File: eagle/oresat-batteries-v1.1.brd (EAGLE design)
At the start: 98.6 x 95.3 mm, 96 parts, among them IC1 74AHC1G08DBV, J2 CORTEX_DEBUG_PTH, Q1 CSD16340Q3, Q2 CSD16340Q3, Q3 TPN4R712MD, Q4 TPN4R712MD, Q5 TPN4R712MD, Q6 TPN4R712MD, Q7 CSD16340Q3, U1 LM3761, U10 LTC4412, U11 MAX17055, U12 LTC4412, U13 LTC4412, U14 STM32F042K6, U15 TCAN330, U2 MC74HC1G04DFT1GOSCT, U3 BQ2970, U4 LTC4411, U5 LTC4411, U6 LTC4411, U7 LTC4411, U8 MC74HC1G04DFT1GOSCT, U9 LTC4412, X1 16MHz

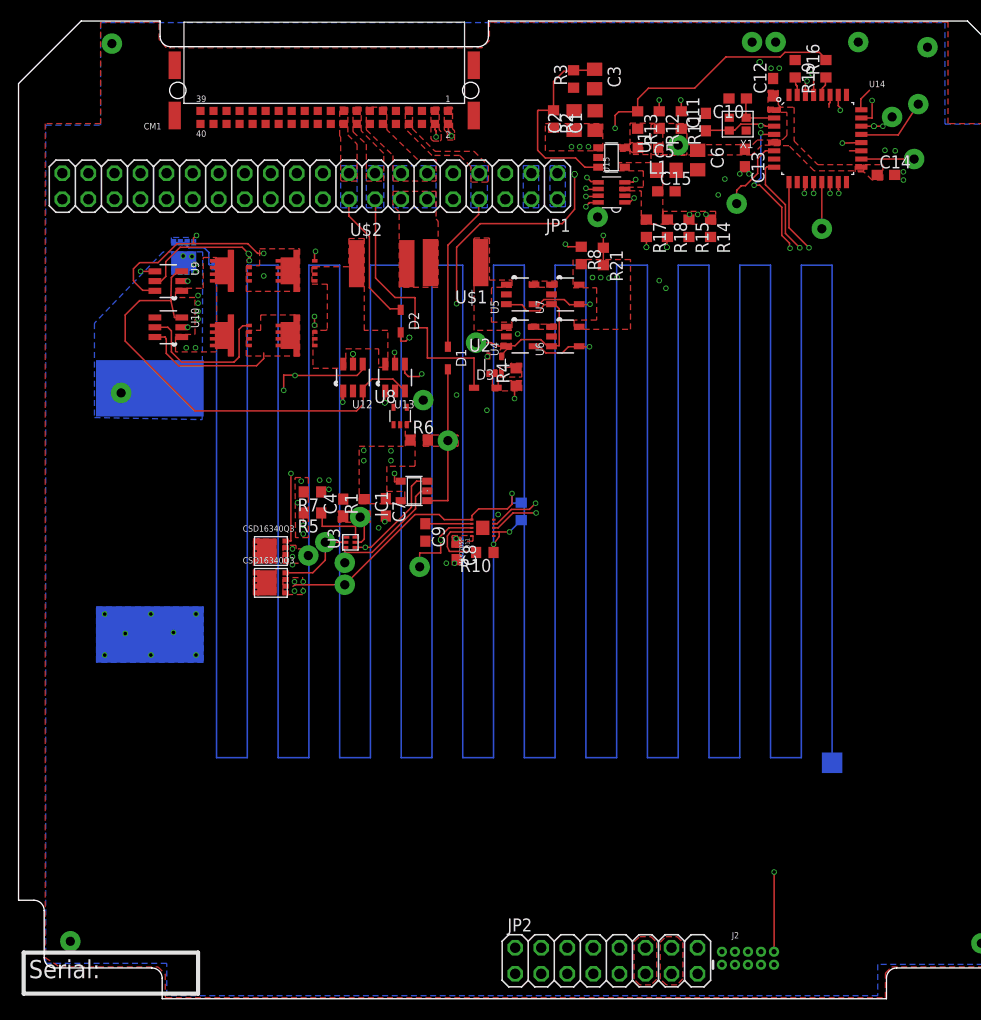
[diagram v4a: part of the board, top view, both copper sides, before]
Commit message: Cosmetics, moved signals to top and bottom layer.
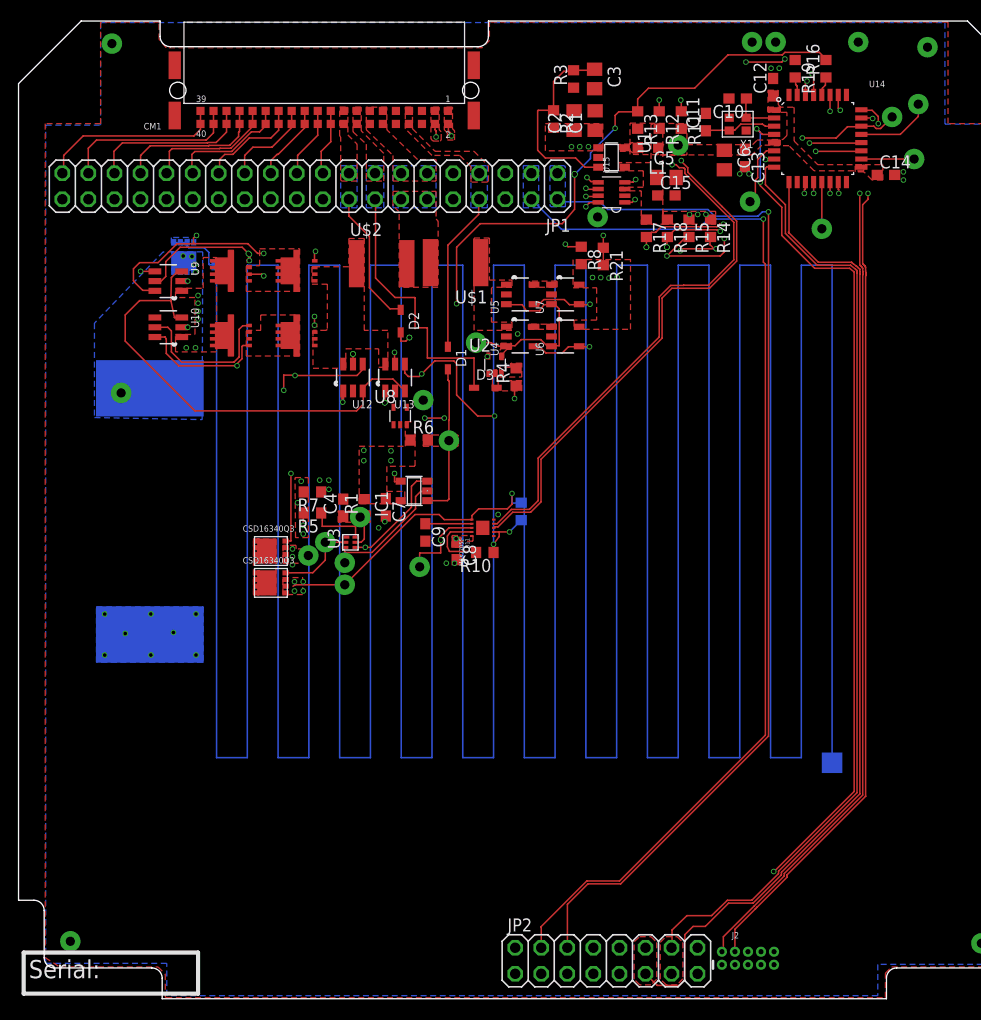
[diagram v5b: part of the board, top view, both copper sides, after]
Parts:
- moved C6 2.60 mm to (68.8, 81.8)
- moved TP24 1.32 mm to (71.3, 77.7)
- moved C5 0.70 mm to (63.1, 80.0)
- moved C15 0.40 mm to (63.1, 78.3)
- moved TP7 0.10 mm to (42.0, 54.4)
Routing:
- net CANH: track 20.3 -> 126.6 mm, vias 2 -> 3
- net CANL: track 17.9 -> 121.1 mm, vias 2 -> 3
- net SPARE11: track 0.00 -> 18.0 mm
- net SPARE10: track 0.00 -> 17.4 mm
- net SPARE9: track 0.00 -> 16.0 mm
- net SPARE8: track 0.00 -> 14.6 mm
- net SPARE7: track 0.00 -> 12.9 mm
- net SPARE6: track 0.00 -> 11.7 mm
- net SPARE5: track 0.00 -> 10.2 mm
- net SDA: track 71.3 -> 80.5 mm, vias 4 -> 3
- net SPARE4: track 0.00 -> 9.06 mm
- net SCL: track 72.7 -> 81.5 mm, vias 6 -> 5
- net SPARE3: track 0.00 -> 7.50 mm
- net SPARE2: track 0.00 -> 6.91 mm
- net SPARE1: track 0.00 -> 6.53 mm
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- added copper zone on layer 15, net 3.3V
- removed copper zone on layer 2, net 3.3V

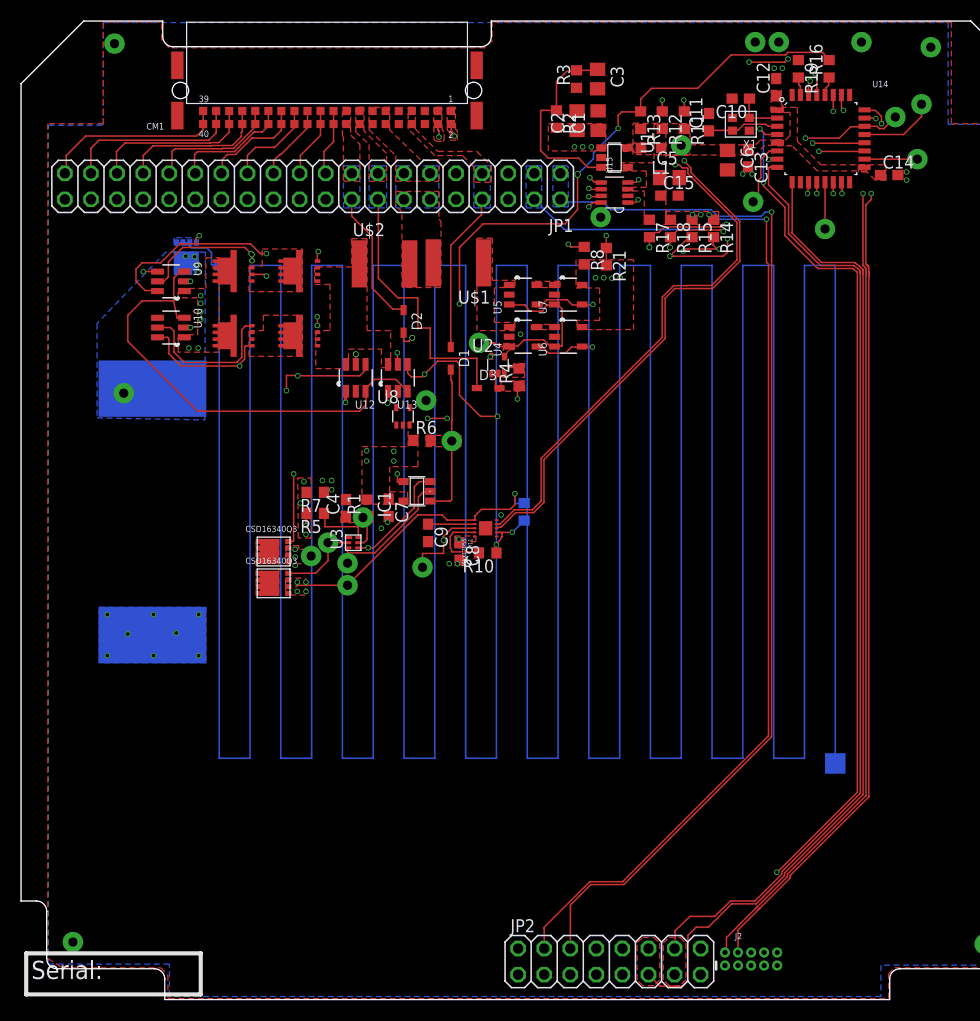
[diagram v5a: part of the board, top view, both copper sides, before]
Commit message: Cosmetics, moved all power and signals from gnd layer
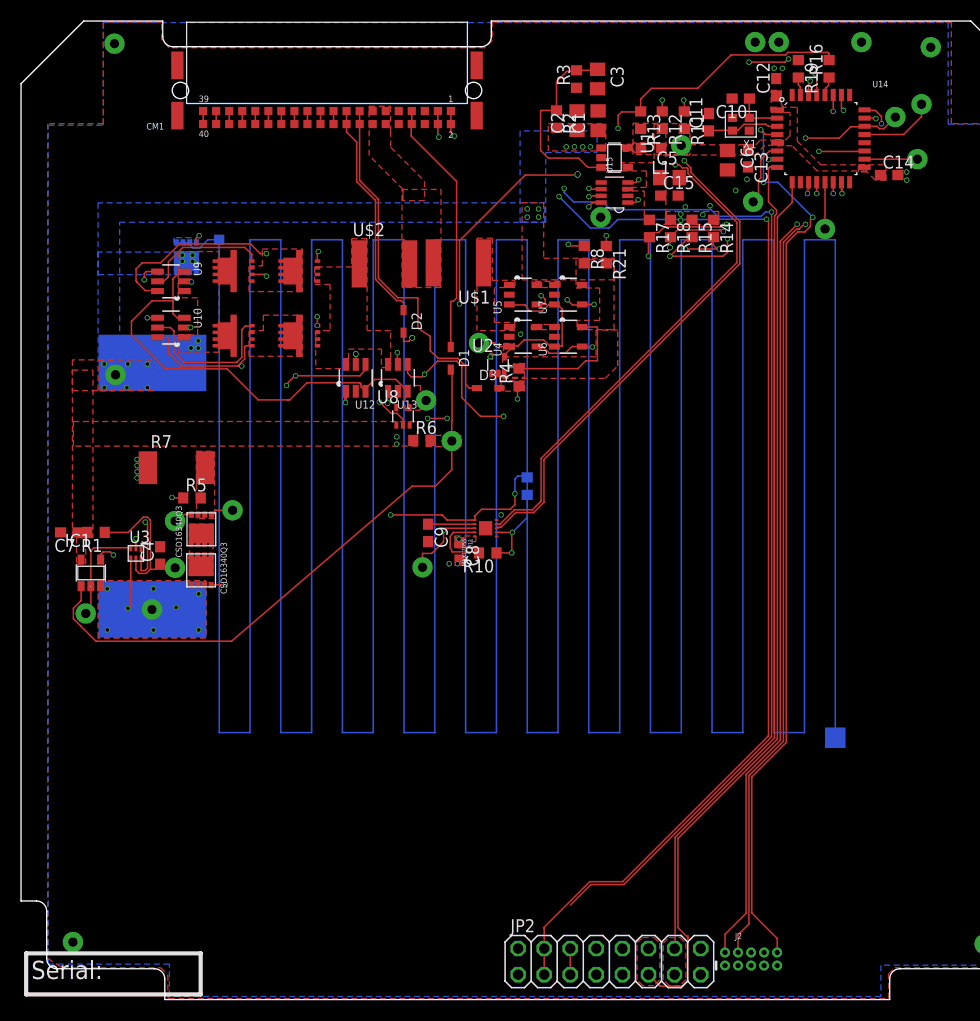
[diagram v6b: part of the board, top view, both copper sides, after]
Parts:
- removed JP1: (no value), pinhead:2X20
- R7: device rcl:R0603 -> rcl:R2512
- moved IC1 32.7 mm to (6.80, 41.5), turned to 0 degrees
- moved C7 31.2 mm to (4.70, 45.5), turned to 180 degrees
- moved R1 26.5 mm to (7.30, 45.5), turned to 180 degrees
- moved TP8 26.0 mm to (6.30, 37.6)
- moved U3 21.2 mm to (11.2, 43.5), turned to 180 degrees
- moved TP5 18.9 mm to (15.0, 42.0)
- moved C4 18.7 mm to (13.6, 43.2)
- moved TP20 16.3 mm to (12.8, 38.0)
- moved TP9 15.0 mm to (15.0, 46.6)
- moved R7 13.7 mm to (15.2, 51.8), turned to 0 degrees
- moved TP13 13.4 mm to (20.6, 47.6)
- moved R5 12.1 mm to (16.6, 48.9), turned to 0 degrees
- moved Q2 8.79 mm to (17.6, 45.8), turned to 180 degrees
- moved Q1 7.30 mm to (17.5, 41.8), turned to 0 degrees
- moved R9 2.52 mm to (49.3, 50.0)
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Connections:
- net !SHUTDOWN: no longer JP1.7, JP1.8
- net CANH: no longer JP1.3, JP1.4
- net CANL: no longer JP1.1, JP1.2
- net CHG_CTL: no longer JP1.15, JP1.16
- net DCHG_CTL: no longer JP1.17, JP1.18
- net GND: no longer JP1.10, JP1.5, JP1.6, JP1.9
- net SPARE1: no longer JP1.19
- net SPARE10: no longer JP1.37
- net SPARE11: no longer JP1.39
- net SPARE2: no longer JP1.21
- net SPARE3: no longer JP1.23
- net SPARE4: no longer JP1.25
- net SPARE5: no longer JP1.27
- net SPARE6: no longer JP1.29
- net SPARE7: no longer JP1.31
- net SPARE8: no longer JP1.33
- net SPARE9: no longer JP1.35
- net VSOLAR: no longer JP1.11, JP1.12, JP1.13, JP1.14
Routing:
- net TO_CHG: track 51.5 -> 117.8 mm
- net SYSSHD: track 14.9 -> 57.3 mm
- net CAN_EN: track 32.0 -> 0.00 mm, vias 2 -> 0
- net SPARE11: track 18.0 -> 1.27 mm
- net SPARE10: track 17.4 -> 1.27 mm
- net SPARE9: track 16.0 -> 1.27 mm
- net SPARE8: track 14.6 -> 1.27 mm
- net V_BATT: track 0.00 -> 13.0 mm, vias 22 -> 24
- net BQBAT: track 3.27 -> 15.6 mm
- net BATT-: track 16.9 -> 4.95 mm, vias 12 -> 8
- net SPARE7: track 12.9 -> 1.27 mm
- net USART2_TX: track 92.8 -> 81.3 mm
- net TO_DCHG: track 58.6 -> 69.8 mm, vias 4 -> 5
- net SPARE6: track 11.7 -> 1.27 mm
- net !SHUTDOWN: track 15.6 -> 25.2 mm
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- added copper zone on layer 1, net DSCHG_SHD
- added copper zone on layer 2, net GND
- added copper zone on layer 15, net V_BATT
- removed copper zone on layer 1, net !SHUTDOWN
- removed copper zone on layer 16, net !SHUTDOWN
- removed copper zone on layer 2, net BATT-
- removed copper zone on layer 1, net BQBAT
- removed copper zone on layer 1, net CANH
- removed copper zone on layer 16, net CANH
- removed copper zone on layer 1, net CANL
- removed copper zone on layer 16, net CANL
- removed copper zone on layer 1, net CHG_CTL
- removed copper zone on layer 16, net CHG_CTL
- removed copper zone on layer 15, net C_SENSE
- removed copper zone on layer 1, net DCHG_CTL
- removed copper zone on layer 16, net DCHG_CTL
- removed copper zone on layer 16, net VSOLAR
- removed copper zone on layer 2, net V_BATT

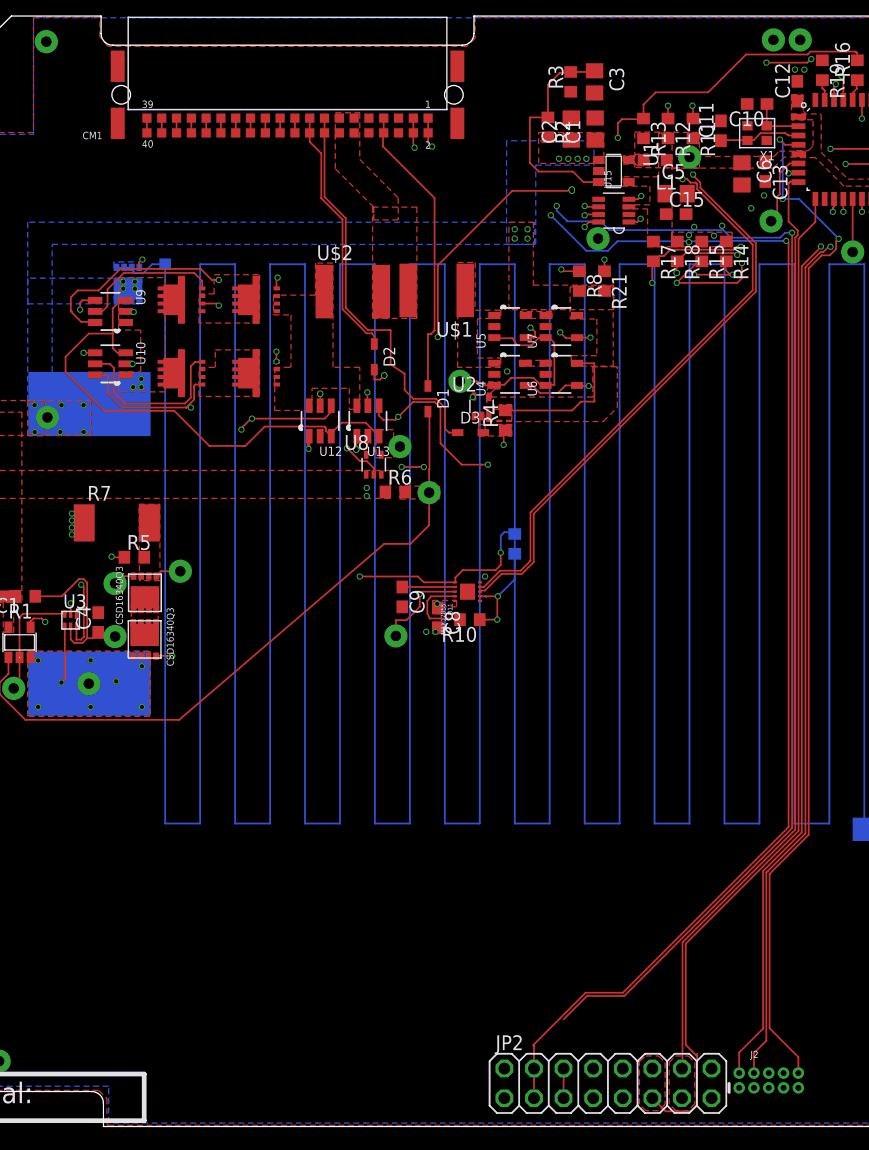
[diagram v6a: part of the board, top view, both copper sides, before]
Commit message: Cleaning, removing airwires.
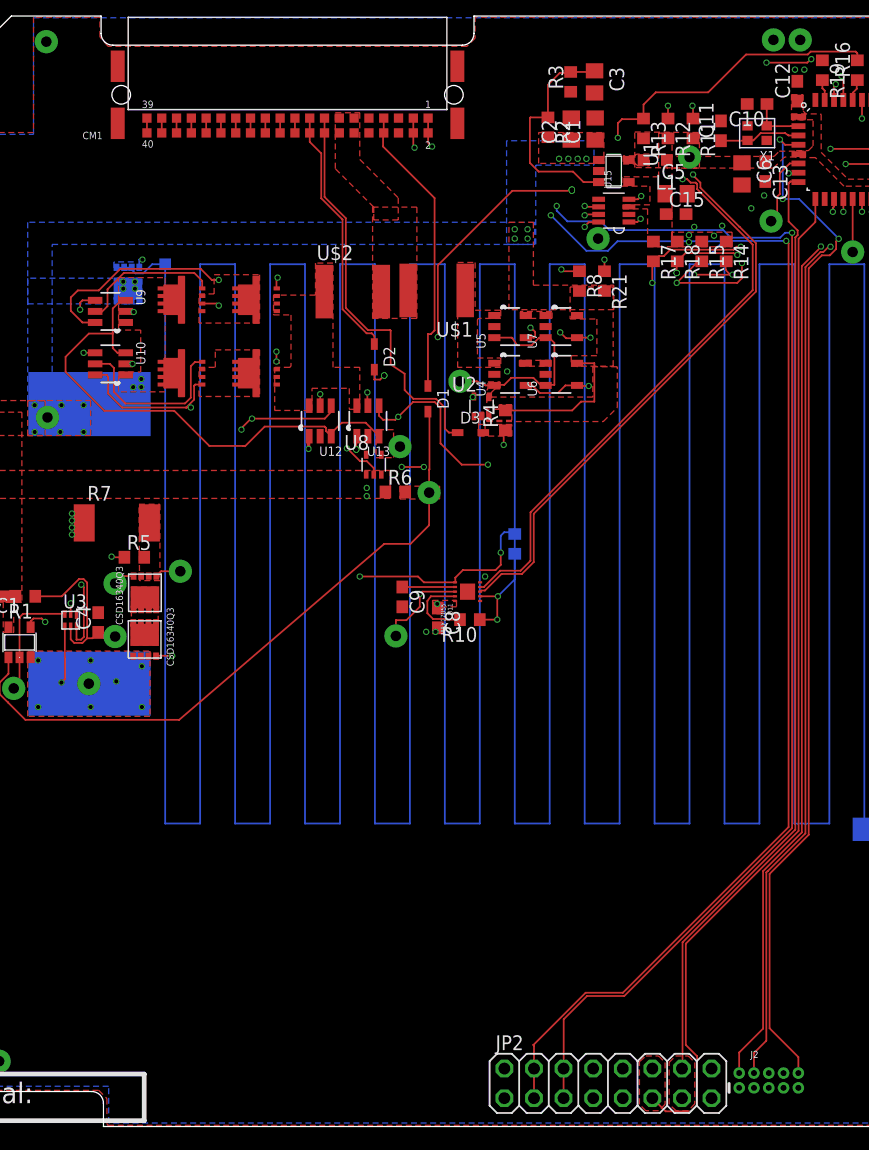
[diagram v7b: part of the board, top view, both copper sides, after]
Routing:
- net CANL: track 120.8 -> 125.2 mm
- net N$12: track 13.1 -> 12.3 mm
- net OSC_IN: track 5.24 -> 4.64 mm
- net N$8: track 15.4 -> 15.5 mm, vias 3 -> 2

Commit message: Cosmetics.
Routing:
- net TO_CHG: track 117.8 -> 58.8 mm
- net CAN_EN: track 0.00 -> 32.5 mm, vias 0 -> 2
